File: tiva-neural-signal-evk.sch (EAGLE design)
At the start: 9 parts, among them IC1 TM4C123G, IC2 TLV70233, X1 USB

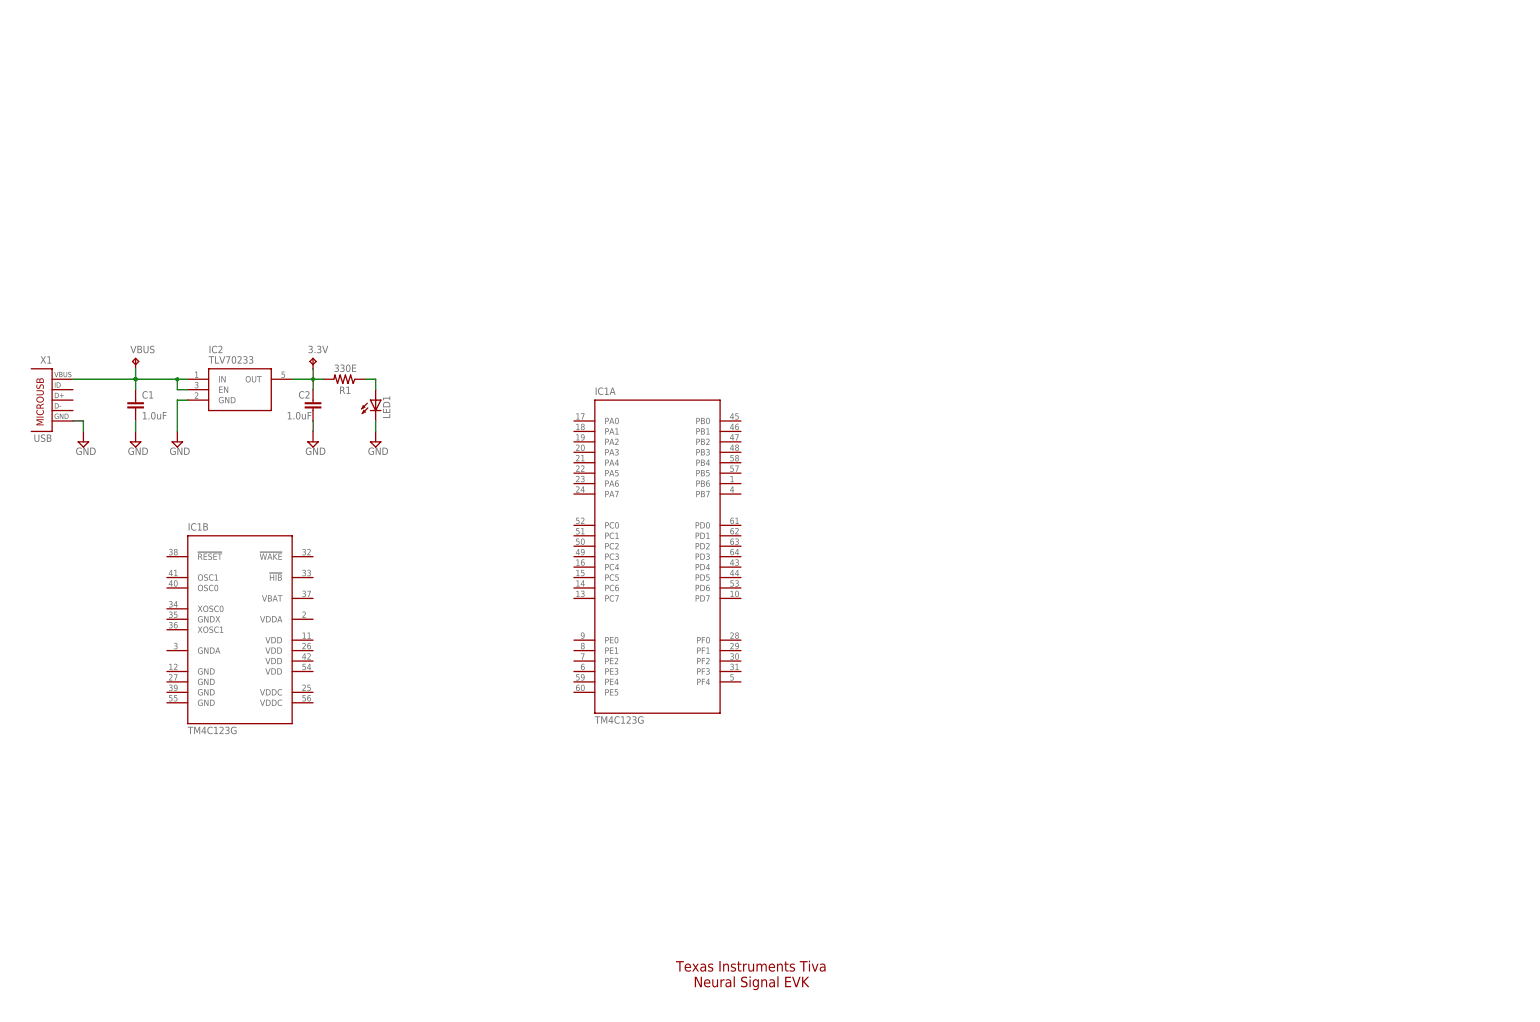
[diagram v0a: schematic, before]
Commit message: added MCU power circuit
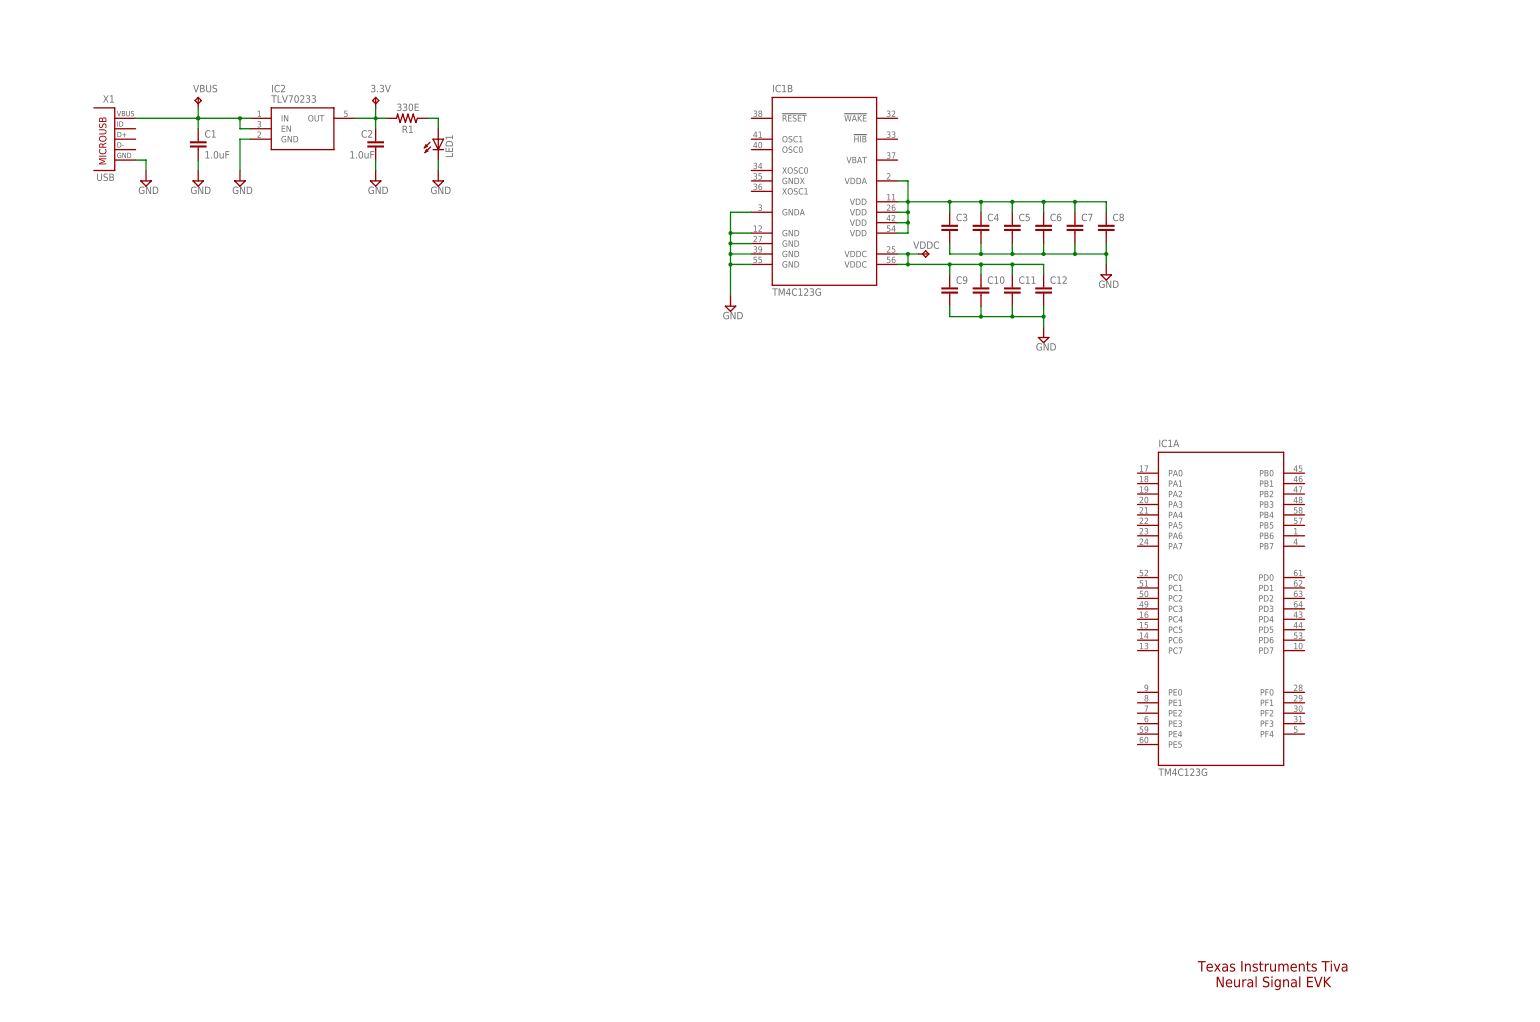
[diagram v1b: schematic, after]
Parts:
- added C10, C11, C12, C3, C4, C5, C6, C7, C8, C9: (no value), rcl:C-EUC0603
- added VDDC: TPB1,27, testpad:TPB1,27
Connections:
- new net N$3: C3.1, C4.1, C5.1, C6.1, C7.1, C8.1, IC1B.VDD@1, IC1B.VDD@2, IC1B.VDD@3, IC1B.VDD@4, IC1B.VDDA
- new net N$4: C10.1, C11.1, C12.1, C9.1, IC1B.VDDC@1, IC1B.VDDC@2, VDDC.TP
- net GND: now also C10.2, C11.2, C12.2, C3.2, C4.2, C5.2, C6.2, C7.2, C8.2, C9.2, IC1B.GND@1, IC1B.GND@2, IC1B.GND@3, IC1B.GND@4, IC1B.GNDA
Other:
- moved on the sheet: 3.3V, C1, C2, IC1A, IC1B, IC2, LED1, R1, VBUS, X1

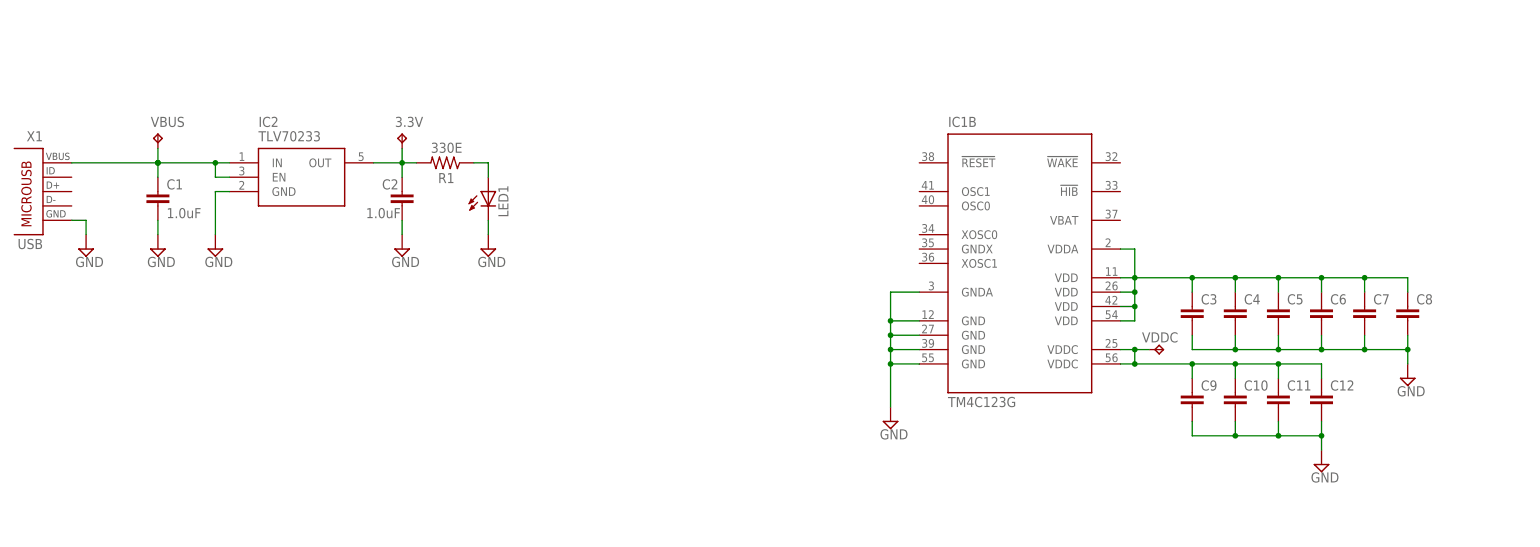
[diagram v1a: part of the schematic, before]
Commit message: completed mcu control
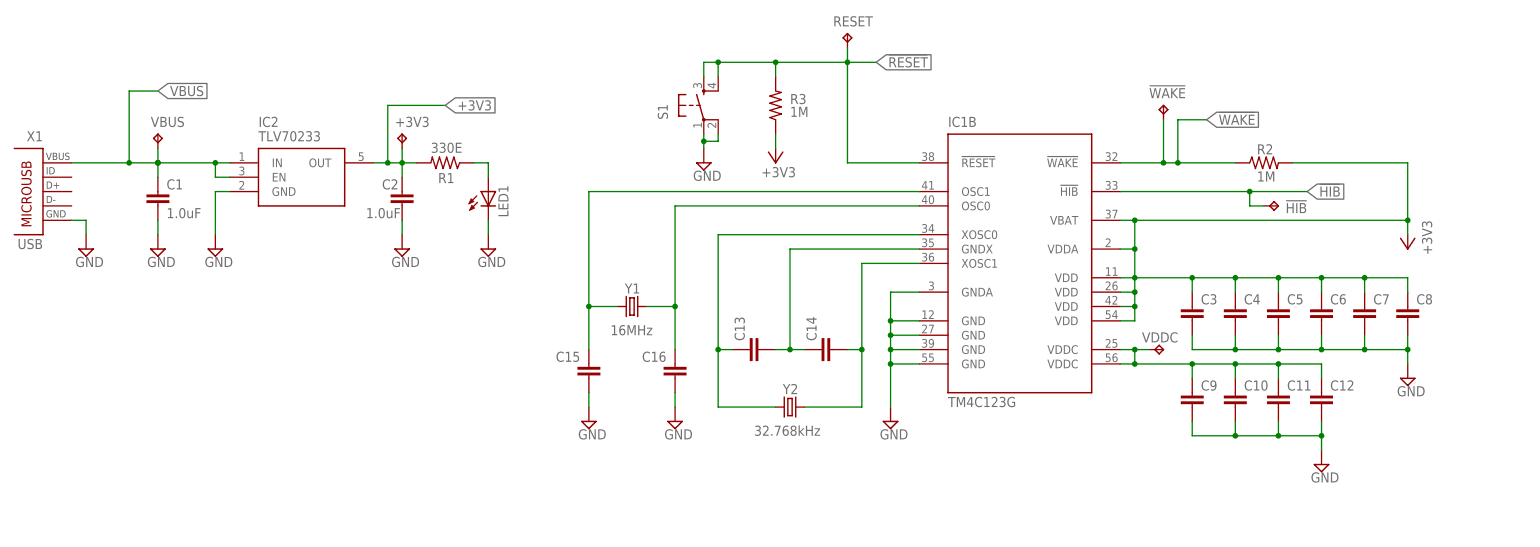
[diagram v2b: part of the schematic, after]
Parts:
- added !HIB!, !WAKE!, RESET: TPB1,27, testpad:TPB1,27
- added C13, C14, C15, C16: (no value), rcl:C-EUC0603
- added R2, R3: 1M, rcl:R-US_R0603
- added S1: (no value), mor307:6MM_SWITCH6MM_SWITCH
- added Y1: 16MHz, SparkFun-FreqCtrl:CRYSTAL5X3
- added Y2: 32.768kHz, SparkFun-FreqCtrl:CRYSTAL32-SMD
- renumbered 3.3V to +3V3
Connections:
- net N$4 renamed VDDC
- removed net N$1: +3V3.TP, C2.1, IC2.OUT, R1.2
- removed net N$3: C3.1, C4.1, C5.1, C6.1, C7.1, C8.1, IC1B.VDD@1, IC1B.VDD@2, IC1B.VDD@3, IC1B.VDD@4, IC1B.VDDA
- new net !HIB!: !HIB!.TP, IC1B.!HIB!
- new net !RESET!: IC1B.!RESET!, R3.2, RESET.TP, S1.S, S1.S1
- new net !WAKE!: !WAKE!.TP, IC1B.!WAKE!, R2.1
- new net +3V3: +3V3.TP, C2.1, C3.1, C4.1, C5.1, C6.1, C7.1, C8.1, IC1B.VBAT, IC1B.VDD@1, IC1B.VDD@2, IC1B.VDD@3, IC1B.VDD@4, IC1B.VDDA, IC2.OUT, R1.2, R2.2, R3.1
- new net N$10: C15.1, IC1B.OSC1, Y1.1
- new net N$6: C14.2, IC1B.XOSC1, Y2.2
- new net N$7: C13.2, C14.1, IC1B.GNDX
- new net N$8: C13.1, IC1B.XOSC0, Y2.1
- new net N$9: C16.1, IC1B.OSC0, Y1.2
- net GND: now also C15.2, C16.2, S1.P, S1.P1

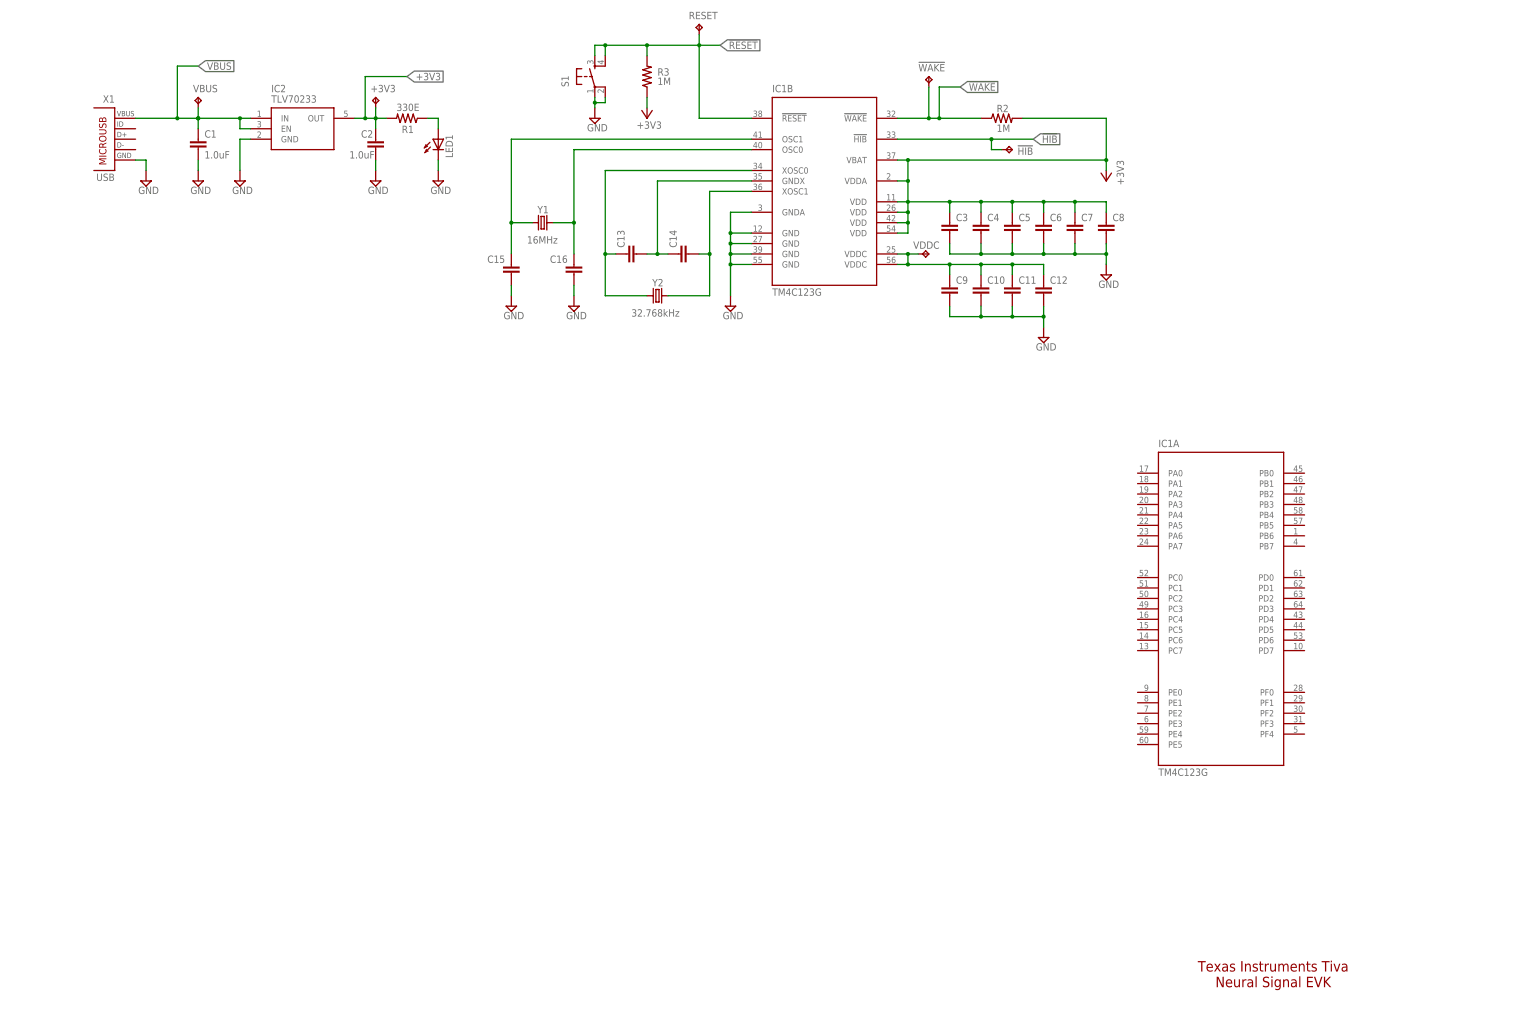
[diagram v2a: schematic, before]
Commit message: added mcu gpio and debug buses
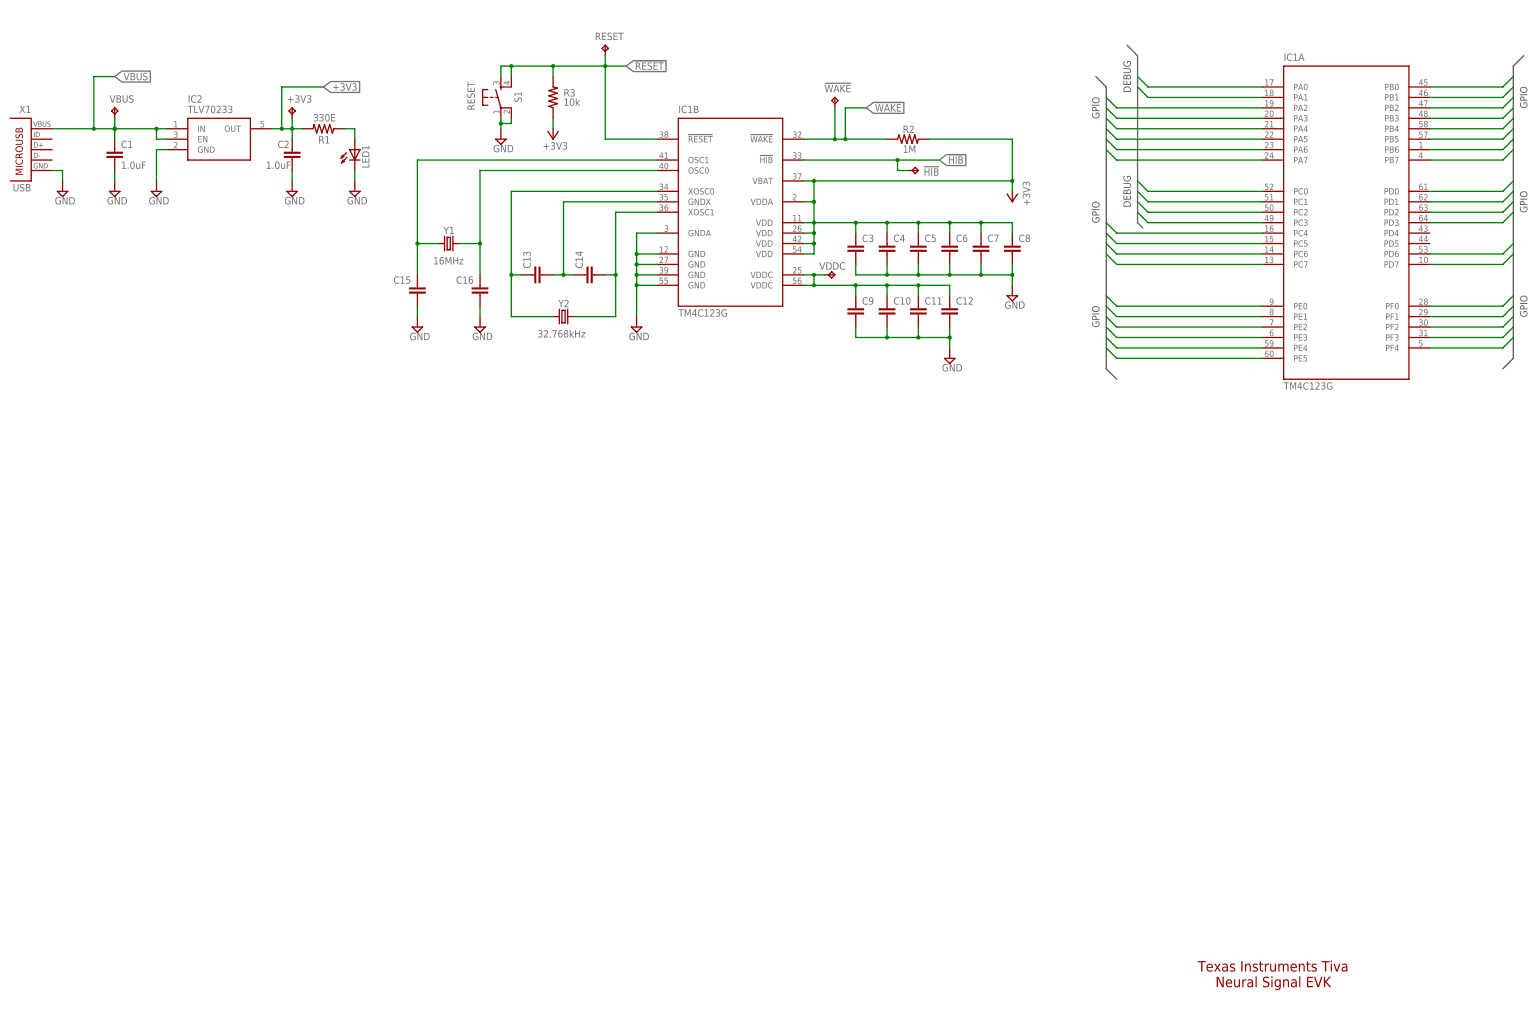
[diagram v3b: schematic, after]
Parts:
- R3: value 1M -> 10k
- S1: value (none) -> RESET
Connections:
- new net PA0: IC1A.PA0
- new net PA1: IC1A.PA1
- new net PA2: IC1A.PA2
- new net PA3: IC1A.PA3
- new net PA4: IC1A.PA4
- new net PA5: IC1A.PA5
- new net PA6: IC1A.PA6
- new net PA7: IC1A.PA7
- new net PB0: IC1A.PB0
- new net PB1: IC1A.PB1
- new net PB2: IC1A.PB2
- new net PB3: IC1A.PB3
- new net PB4: IC1A.PB4
- new net PB5: IC1A.PB5
- new net PB6: IC1A.PB6
- new net PB7: IC1A.PB7
- new net PC0: IC1A.PC0
- new net PC1: IC1A.PC1
- new net PC2: IC1A.PC2
- new net PC3: IC1A.PC3
- new net PC4: IC1A.PC4
- new net PC5: IC1A.PC5
- new net PC6: IC1A.PC6
- new net PC7: IC1A.PC7
- new net PD0: IC1A.PD0
- new net PD1: IC1A.PD1
- new net PD2: IC1A.PD2
- new net PD3: IC1A.PD3
- new net PD6: IC1A.PD6
- new net PD7: IC1A.PD7
- new net PE0: IC1A.PE0
- new net PE1: IC1A.PE1
- new net PE2: IC1A.PE2
- new net PE3: IC1A.PE3
- new net PE4: IC1A.PE4
- new net PE5: IC1A.PE5
- new net PF0: IC1A.PF0
- new net PF1: IC1A.PF1
- new net PF2: IC1A.PF2
- new net PF3: IC1A.PF3
- new net PF4: IC1A.PF4
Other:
- note added: "DEBUG"
- note added: "GPIO"
- moved on the sheet: +3V3, C1, C10, C11, C12, C13, C14, C15, C16, C2, C3, C4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
